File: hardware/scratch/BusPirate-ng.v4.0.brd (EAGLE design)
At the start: 80 x 49 mm, 134 parts, among them CON1 CON-USB-F-MICRO-B, IC1 IC_UC_STM32F103RBTXX-LQFP64, IC10 74LVC1G07DBV, IC11 IC_BUFF_SN74LVC1T45DBV, IC12 74LVC1G07DBV, IC13 IC_BUFF_SN74LVC1T45DBV, IC14 74LVC1G07DBV, IC15 IC_BUFF_SN74LVC1T45DBV, IC16 74LVC1G07DBV, IC17 IC_BUFF_SN74LVC1T45DBV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

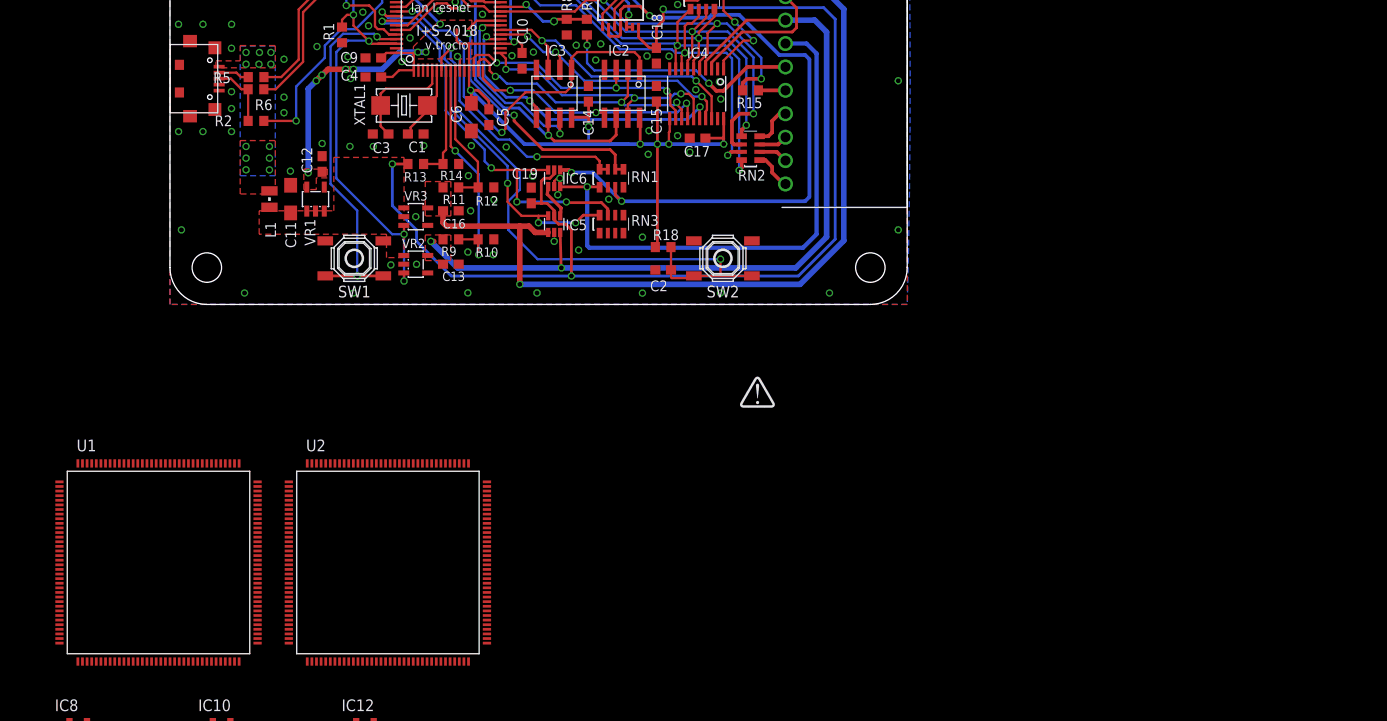
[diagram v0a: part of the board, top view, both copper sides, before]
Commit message: connect ARM chip's FSMC address, data and control pins except CS to FPGA
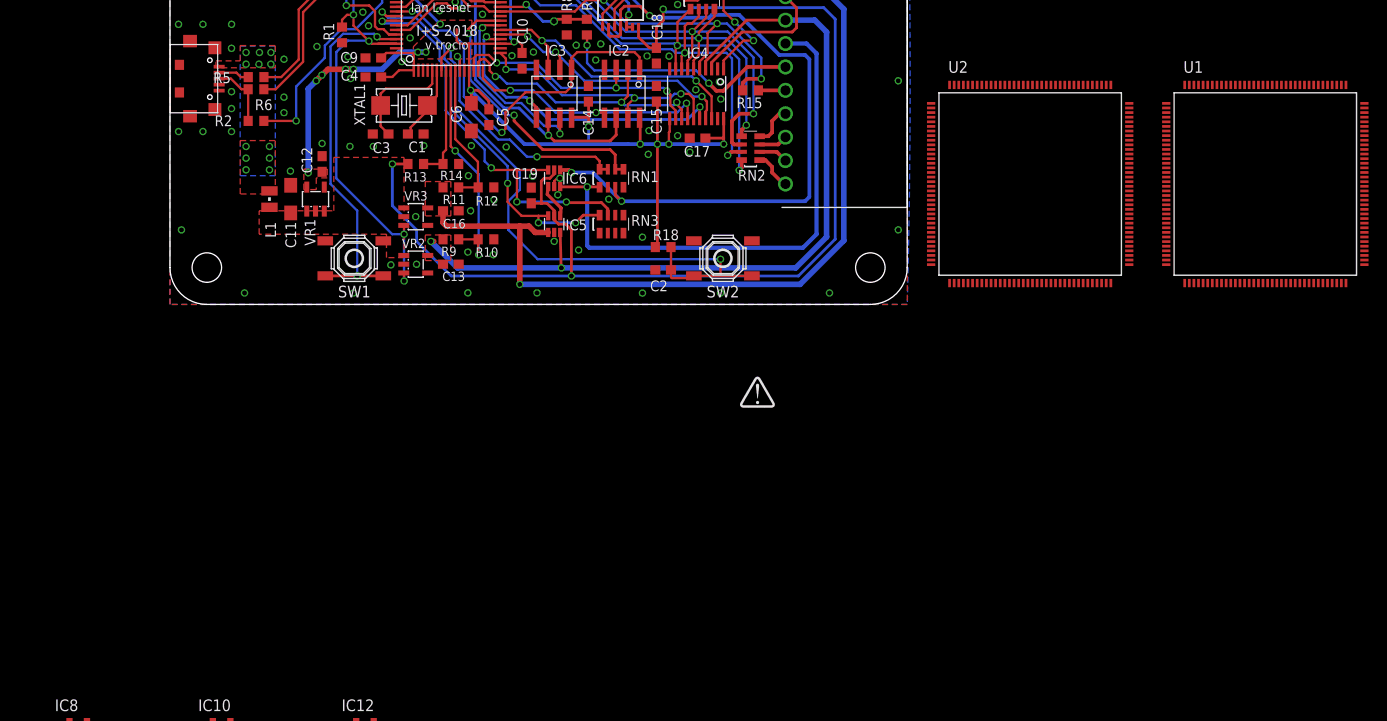
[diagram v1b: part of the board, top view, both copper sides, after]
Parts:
- moved U1 126.9 mm to (118.9, 13.1)
- moved U2 80.9 mm to (93.3, 13.1)
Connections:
- net FSMC_A0: now also U1.10
- net FSMC_A1: now also U1.11
- net FSMC_A2: now also U1.12
- net FSMC_A3: now also U1.15
- net FSMC_A4: now also U1.16
- net FSMC_A5: now also U1.17
- net FSMC_D0: now also U1.24
- net FSMC_D1: now also U1.23
- net FSMC_D2: now also U1.1
- net FSMC_D3: now also U1.2
- net FSMC_D4: now also U1.25
- net FSMC_D5: now also U1.26
- net FSMC_D6: now also U1.28
- net FSMC_D7: now also U1.29
- net FSMC_NOE_OE: now also U1.20
- net FSMC_NWE_WE: now also U1.21

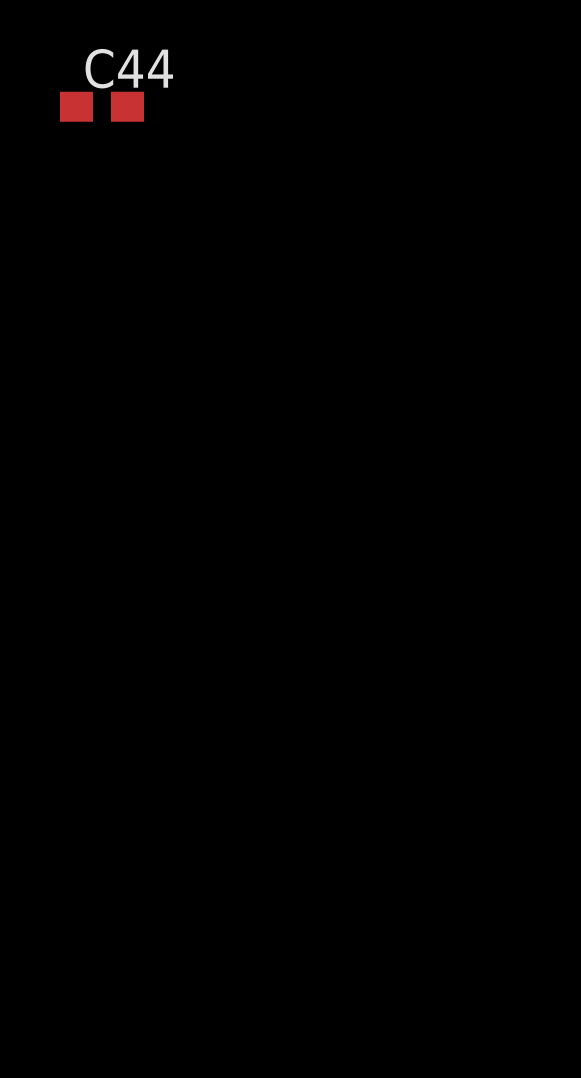
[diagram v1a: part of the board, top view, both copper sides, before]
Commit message: connect power 1.2V and 3.3V for bank 2 and 3 of FPGA
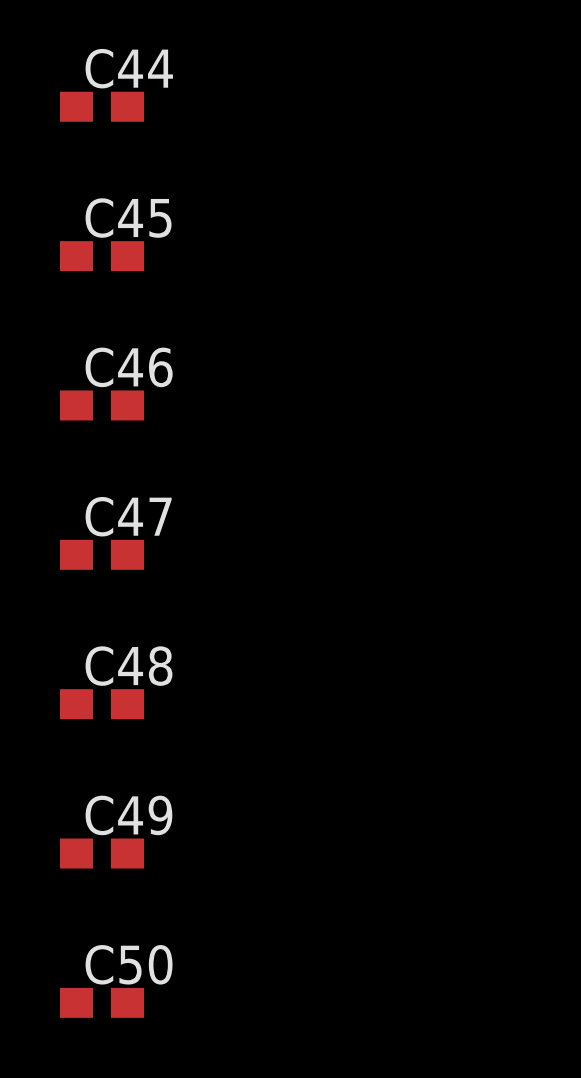
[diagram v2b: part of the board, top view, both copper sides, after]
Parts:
- added C45, C46, C47, C48, C49, C50: 0.1uF, rcl:C0603
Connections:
- removed net VCCIO_2: U1.46, U1.57
- removed net VCCIO_3: U1.30, U1.6
- net 1V2: now also C45.2, C48.2, U1.27, U1.40
- net 3V3: now also C46.2, C47.2, C49.2, C50.2, U1.30, U1.46, U1.57, U1.6; no longer U1.27, U1.40
- net GND: now also C45.1, C46.1, C47.1, C48.1, C49.1, C50.1

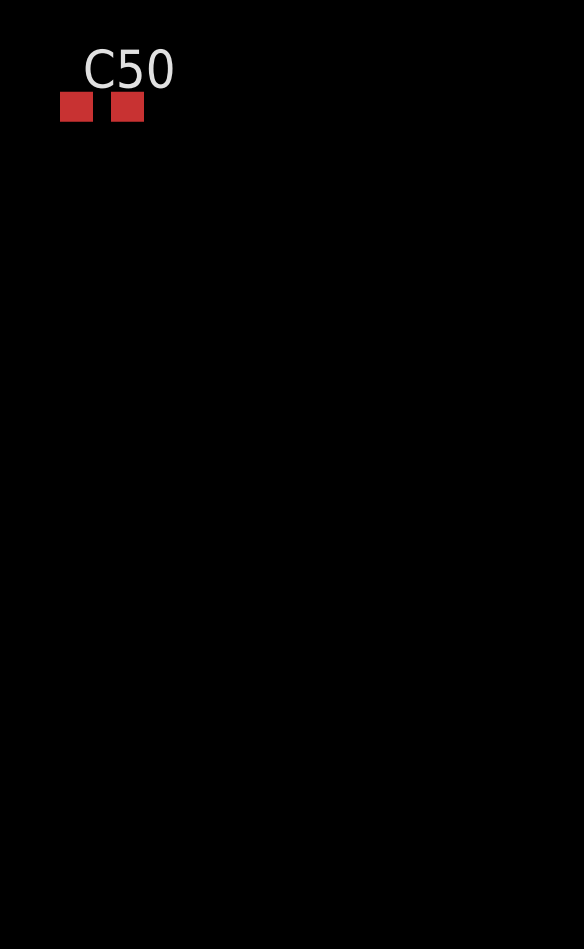
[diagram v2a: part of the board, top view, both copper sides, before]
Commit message: wired -BOOT0 and BOOT1 to corresponding switches -NRST to reset switch -VBAT with 0.1uF cap to 3V3 -VDDA with 0.1uF and 1uF cap to 3V3 -VSSA to GND -PC0 - PC4 to ADC2 - AD6 -control pins pull ups VEXTPU, IO_OE, LD1 and USBLED -PB0 to AUX0 -PB1 to ADC1 -control pins PB3, PB4, PB5 and PB6 to SRAM_CS, V50PU, V33PU and VREGEN respectively -UART TX and UART RX to PA9 and PA10 -programming pins SWDIO and SWCLK to PA13 and PA14 -USB detect to PA15
added connection but not wired yet to FPGA
-FSMC_D8 to D15
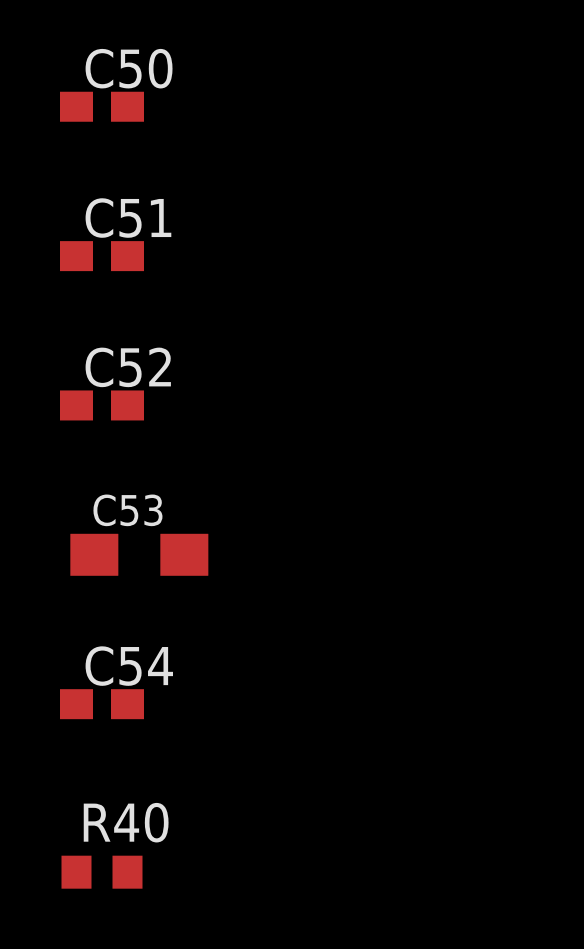
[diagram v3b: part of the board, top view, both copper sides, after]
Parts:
- added C51, C52, C54: 0.1uF, rcl:C0603
- added C53: 1uF, rcl:SMC_A
- added R40: 10K, dp_devices:R603
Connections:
- new net FSMC_D10: U2.66
- new net FSMC_D11: U2.67
- new net FSMC_D12: U2.68
- new net FSMC_D13: U2.77
- new net FSMC_D14: U2.78
- new net FSMC_D15: U2.79
- new net FSMC_D8: U2.64
- new net FSMC_D9: U2.65
- net 3V3: now also C52.2, C53.+, C54.2, U2.33, U2.6
- net ADC1: now also U2.47
- net ADC2: now also U2.29
- net ADC3: now also U2.27
- net ADC4: now also U2.28
- net ADC5: now also U2.26
- net ADC6: now also U2.44
- net AUX0: now also U2.46
- net BOOT0: now also U2.138
- net BOOT1: now also U2.48
- net GND: now also C51.1, C52.1, C53.-, C54.1, R40.2, U2.30
- net IO_OE: now also U2.97
- net LD1: now also U2.98
- net RST: now also C51.2, U2.25
- net SRAM_CS: now also U2.133
- net SWCLK: now also U2.109
- net SWDIO: now also U2.105
- net UART_RX: now also U2.102
- net UART_TX: now also U2.101
- net USBLED: now also U2.99
- net USB_DET: now also U2.110
- net V33PU: now also U2.135
- net V50PU: now also U2.134
- net VEXTPU: now also U2.96
- net VREGEN: now also R40.1, U2.136

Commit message: removed connection FSMC_NOE_OE and FSMC_NEW_WE wired FSMC_D8 - FSMC_D15 to FPGA
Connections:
- new net N$11: U1.3
- new net N$15: U1.4
- new net N$17: U1.34
- new net N$19: U1.7
- new net N$21: U1.8
- new net N$22: U1.9
- net FSMC_D10: now also U1.26
- net FSMC_D11: now also U1.28
- net FSMC_D12: now also U1.29
- net FSMC_D13: now also U1.33
- net FSMC_D14: now also U1.32
- net FSMC_D15: now also U1.31
- net FSMC_D4: now also U1.18; no longer U1.25
- net FSMC_D5: now also U1.19; no longer U1.26
- net FSMC_D6: now also U1.20; no longer U1.28
- net FSMC_D7: now also U1.21; no longer U1.29
- net FSMC_D8: now also U1.22
- net FSMC_D9: now also U1.25
- net FSMC_NOE_OE: no longer U1.20
- net FSMC_NWE_WE: no longer U1.21
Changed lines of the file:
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@@
 <signal name="FSMC_NOE_OE">
 <contactref element="U2" pad="118"/>
-<contactref element="U1" pad="20"/>
-<wire x1="108.1093" y1="12.3183" x2="97.595" y2="23.8183" width="0" layer="19" extent="1-1"/>
 </signal>
 <signal name="FSMC_NWE_WE">
 <contactref element="U2" pad="119"/>
-<contactref element="U1" pad="21"/>
-<wire x1="108.1093" y1="11.8183" x2="97.095" y2="23.8183" width="0" layer="19" extent="1-1"/>
 </signal>
 <signal name="FSMC_D0">
@@
 <signal name="FSMC_D4">
 <contactref element="U2" pad="58"/>
-<contactref element="U1" pad="25"/>
-<wire x1="95.095" y1="2.3183" x2="108.1093" y2="9.8183" width="0" layer="19" extent="1-1"/>
+<contactref element="U1" pad="18"/>
+<wire x1="95.095" y1="2.3183" x2="108.1093" y2="13.3183" width="0" layer="19" extent="1-1"/>
 </signal>
 <signal name="FSMC_D5">
 <contactref element="U2" pad="59"/>
-<contactref element="U1" pad="26"/>
-<wire x1="95.595" y1="2.3183" x2="108.1093" y2="9.3183" width="0" layer="19" extent="1-1"/>
+<contactref element="U1" pad="19"/>
+<wire x1="95.595" y1="2.3183" x2="108.1093" y2="12.8183" width="0" layer="19" extent="1-1"/>
 </signal>
 <signal name="FSMC_D6">
 <contactref element="U2" pad="60"/>
-<contactref element="U1" pad="28"/>
-<wire x1="96.095" y1="2.3183" x2="108.1093" y2="8.3183" width="0" layer="19" extent="1-1"/>
+<contactref element="U1" pad="20"/>
+<wire x1="96.095" y1="2.3183" x2="108.1093" y2="12.3183" width="0" layer="19" extent="1-1"/>
 </signal>
 <signal name="FSMC_D7">
 <contactref element="U2" pad="63"/>
-<contactref element="U1" pad="29"/>
-<wire x1="97.595" y1="2.3183" x2="108.1093" y2="7.8183" width="0" layer="19" extent="1-1"/>
+<contactref element="U1" pad="21"/>
+<wire x1="97.595" y1="2.3183" x2="108.1093" y2="11.8183" width="0" layer="19" extent="1-1"/>
 </signal>
 <signal name="FSMC_NE3_CE">
@@
 <signal name="FSMC_D8">
 <contactref element="U2" pad="64"/>
+<contactref element="U1" pad="22"/>
+<wire x1="98.095" y1="2.3183" x2="108.1093" y2="11.3183" width="0" layer="19" extent="1-1"/>
 </signal>
 <signal name="FSMC_D9">
 <contactref element="U2" pad="65"/>
+<contactref element="U1" pad="25"/>
+<wire x1="98.595" y1="2.3183" x2="108.1093" y2="9.8183" width="0" layer="19" extent="1-1"/>
 </signal>
 <signal name="FSMC_D10">
 <contactref element="U2" pad="66"/>
+<contactref element="U1" pad="26"/>
+<wire x1="99.095" y1="2.3183" x2="108.1093" y2="9.3183" width="0" layer="19" extent="1-1"/>
 </signal>
 <signal name="FSMC_D11">
 <contactref element="U2" pad="67"/>
+<contactref element="U1" pad="28"/>
+<wire x1="99.595" y1="2.3183" x2="108.1093" y2="8.3183" width="0" layer="19" extent="1-1"/>
 </signal>
 <signal name="FSMC_D12">
 <contactref element="U2" pad="68"/>
+<contactref element="U1" pad="29"/>
+<wire x1="100.095" y1="2.3183" x2="108.1093" y2="7.8183" width="0" layer="19" extent="1-1"/>
 </signal>
 <signal name="FSMC_D13">
 <contactref element="U2" pad="77"/>
+<contactref element="U1" pad="33"/>
+<wire x1="104.095" y1="6.3183" x2="108.1093" y2="5.8183" width="0" layer="19" extent="1-1"/>
 </signal>
 <signal name="FSMC_D14">
 <contactref element="U2" pad="78"/>
+<contactref element="U1" pad="32"/>
+<wire x1="104.095" y1="6.8183" x2="108.1093" y2="6.3183" width="0" layer="19" extent="1-1"/>
 </signal>
 <signal name="FSMC_D15">
 <contactref element="U2" pad="79"/>
+<contactref element="U1" pad="31"/>
+<wire x1="104.095" y1="7.3183" x2="108.1093" y2="6.8183" width="0" layer="19" extent="1-1"/>
+</signal>
+<signal name="N$17">
+<contactref element="U1" pad="34"/>
+</signal>
+<signal name="N$11">
+<contactref element="U1" pad="3"/>
+</signal>
+<signal name="N$15">
+<contactref element="U1" pad="4"/>
+</signal>
+<signal name="N$19">
+<contactref element="U1" pad="7"/>
+</signal>
+<signal name="N$21">
+<contactref element="U1" pad="8"/>
+</signal>
+<signal name="N$22">
+<contactref element="U1" pad="9"/>
 </signal>
 </signals>
